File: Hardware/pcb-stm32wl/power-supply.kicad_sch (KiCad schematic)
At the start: 33 parts, among them J2 JST-PH, Q1 PMV32UP,215, U1 TPS22917DBV, U12 TPS22917DBV, U2 TPS3839G18DBZT‎, U4 RP605Z283B

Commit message: all new components placed, not wired
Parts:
- added C22: 18123D106KAT2A, CAP_1812Z_AVX, symbol 18123D106KAT2A-10uF-BC:18123D106KAT2A
- added C25: T520V686M010ATE045, CAPMP7.6X4.3_1.9N_KEM, symbol T520V686M010ATE045-68uF-BC:T520V686M010ATE045
- added CR1: B0530W-7-F, SOD123_DIO, symbol B0530W-7-F-BC-DIODE:B0530W-7-F
- added U8: MAX1837ETT50+T, 21-0137I_T1033-1_MXM, symbol MAX1837ETT50_T-bc-5V:MAX1837ETT50+T
- added U9: WE-TPC_5828, WE-TPC_5828:WE-TPC_5828, symbol 744053470-47uF-BC:WE-TPC_5828
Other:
- note added: "Buck-Boost Converter(2.7V - Vout)"
- note added: "Buck-Boost Converter(5V - Vout)"
- note removed: "Buck-Boost Converter"
- moved on the sheet: C51, R25, U12

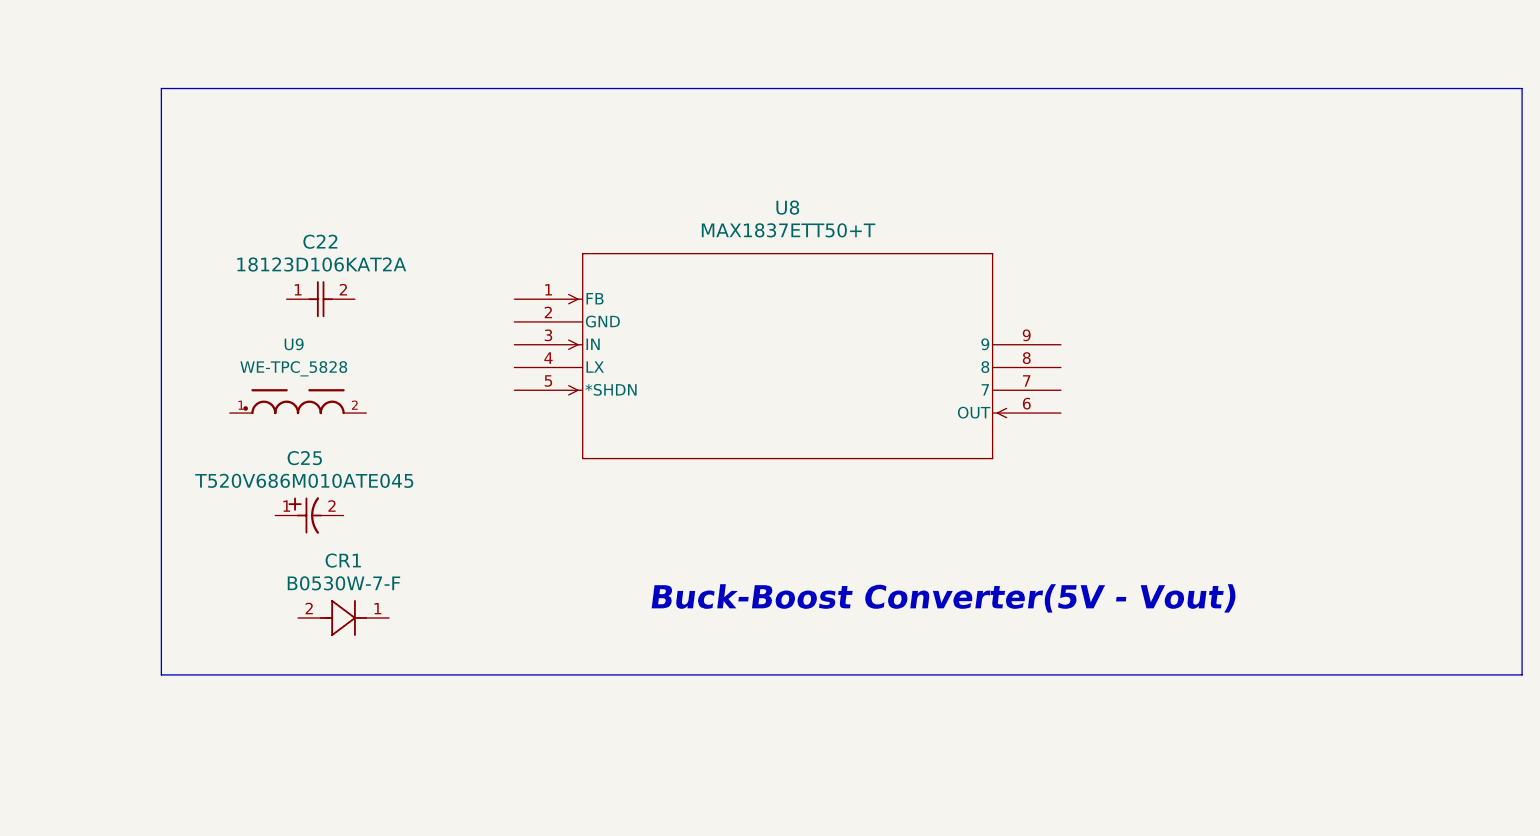
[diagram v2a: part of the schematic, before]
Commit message: added footprints to all newly selected components.
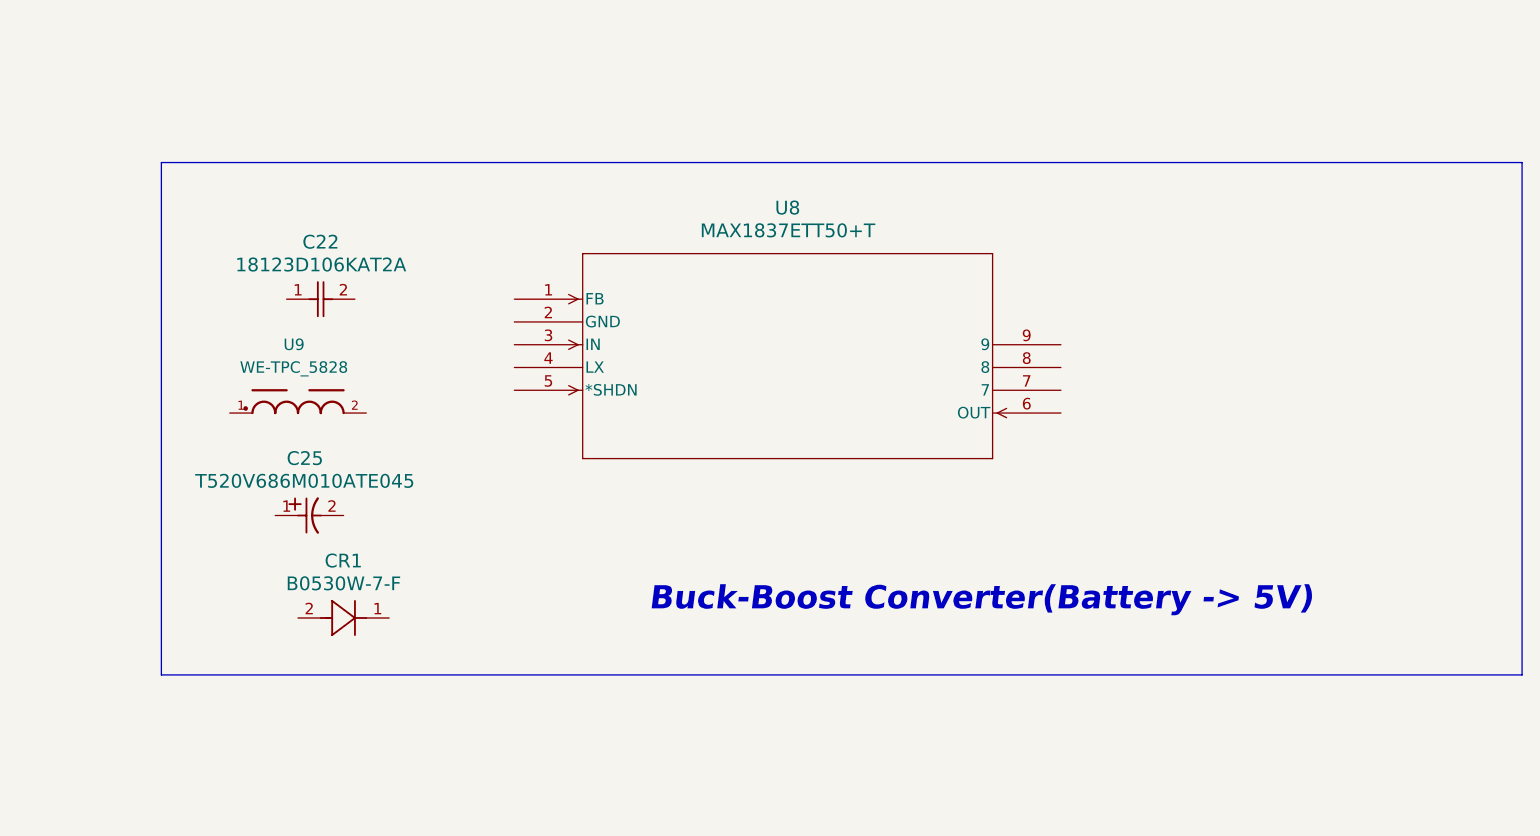
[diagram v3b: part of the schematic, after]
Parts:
- C22: Distributor link (none) -> https://www.digikey.ca/en/products/detail/kyocera-avx/18123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; Manufacturer (none) -> KYOCERA AVX; Manufacturer Part Number (none) -> 18123D106KAT2A
- C25: Distributor link (none) -> https://www.digikey.ca/en/products/detail/kemet/T520V686M01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; Manufacturer (none) -> KEMET; Manufacturer Part Number (none) -> T520V686M010ATE045
- CR1: Distributor link (none) -> https://www.digikey.ca/en/products/detail/diodes-incorporat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; Manufacturer (none) -> Diodes Incorporated; Manufacturer Part Number (none) -> B0530W-7-F
- U8: Distributor link (none) -> https://www.digikey.com/en/products/detail/analog-devices-i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; Manufacturer (none) -> Analog devices; Manufacturer Part Number (none) -> MAX1837ETT50+T
- U9: Distributor link (none) -> https://www.digikey.com/en/products/detail/w%C3%BCrth-elekt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; Manufacturer (none) -> Würth Elektronik; Manufacturer Part Number (none) -> 744053470
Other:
- note added: "Buck-Boost Converter(Battery -> 5V)"
- note removed: "Buck-Boost Converter(5V - Vout)"
